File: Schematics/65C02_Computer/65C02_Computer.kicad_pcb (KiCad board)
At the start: 2 copper layers, 203.2 x 149.9 mm, 60 parts, among them J1 CLK Jumper, J2 Expansion port, J3 USB_B_Micro, J4 LCD Connector, J5 VIA2PA, J6 VIA2PB, J7 Mini-DIN-6, SW1 RESET, U1 74HC02, U10 FT230XS, U11 65C51N, U12 ATtiny4313-PU, U2 28C256, U3 65C02S, U4 74HC00, U5 74HC21, U6 62256, U7 NE555, U8 65C22S, U9 65C22S, X1 1MHz, X2 1.8432MHz

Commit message: Further updates to schematic
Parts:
- added R13: 4K7, Resistor_THT:R_Axial_DIN0207_L6.3mm_D2.5mm_P7.62mm_Horizontal, F.Cu at (137.5, 134.7)
- R1, R2, R4: value 3K3 -> 4K7
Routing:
- net +5V: track 295.5 -> 0.00 mm, vias 1 -> 0
- net a1: track 223.4 -> 0.00 mm
- net d4: track 223.4 -> 0.00 mm
- net a0: track 221.3 -> 0.00 mm, vias 2 -> 0
- net d5: track 220.5 -> 0.00 mm
- net d1: track 217.5 -> 0.00 mm
- net d6: track 216.0 -> 0.00 mm
- net d0: track 214.8 -> 0.00 mm
- net d2: track 214.1 -> 0.00 mm
- net a10: track 213.1 -> 0.00 mm
- net d7: track 212.5 -> 0.00 mm
- net d3: track 210.5 -> 0.00 mm
- net CLK: track 110.3 -> 0.00 mm, vias 2 -> 0
- net R~W: track 109.4 -> 0.00 mm, vias 3 -> 0
- net ~IOCS: track 106.3 -> 0.00 mm, vias 2 -> 0
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- removed copper zone on F.Cu, net GND

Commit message: Moved things around PCB
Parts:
- removed the REF** at (83.5, 205.5)
- moved C7 104.1 mm to (200.7, 78.7), turned to 270 degrees
- moved R13 100.6 mm to (193.0, 50.8)
- moved R6 86.2 mm to (143.5, 38.1), turned to 90 degrees
- moved C10 80.0 mm to (155.0, 50.8)
- moved R5 79.1 mm to (137.2, 38.1), turned to 90 degrees
- moved U5 79.0 mm to (40.6, 27.9)
- moved X1 77.9 mm to (33.0, 68.6)
- moved C6 76.4 mm to (73.7, 27.9), turned to 270 degrees
- moved J2 76.0 mm to (106.7, 53.3)
- moved R3 72.4 mm to (130.8, 38.1), turned to 90 degrees
- moved C8 70.3 mm to (137.2, 45.7), turned to 0 degrees
- moved C9 69.4 mm to (53.3, 28.0), turned to 270 degrees
- moved C4 62.6 mm to (128.3, 45.7), turned to 180 degrees
- moved U7 59.8 mm to (116.8, 38.1), turned to 90 degrees
- moved U1 59.2 mm to (81.3, 27.9)
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
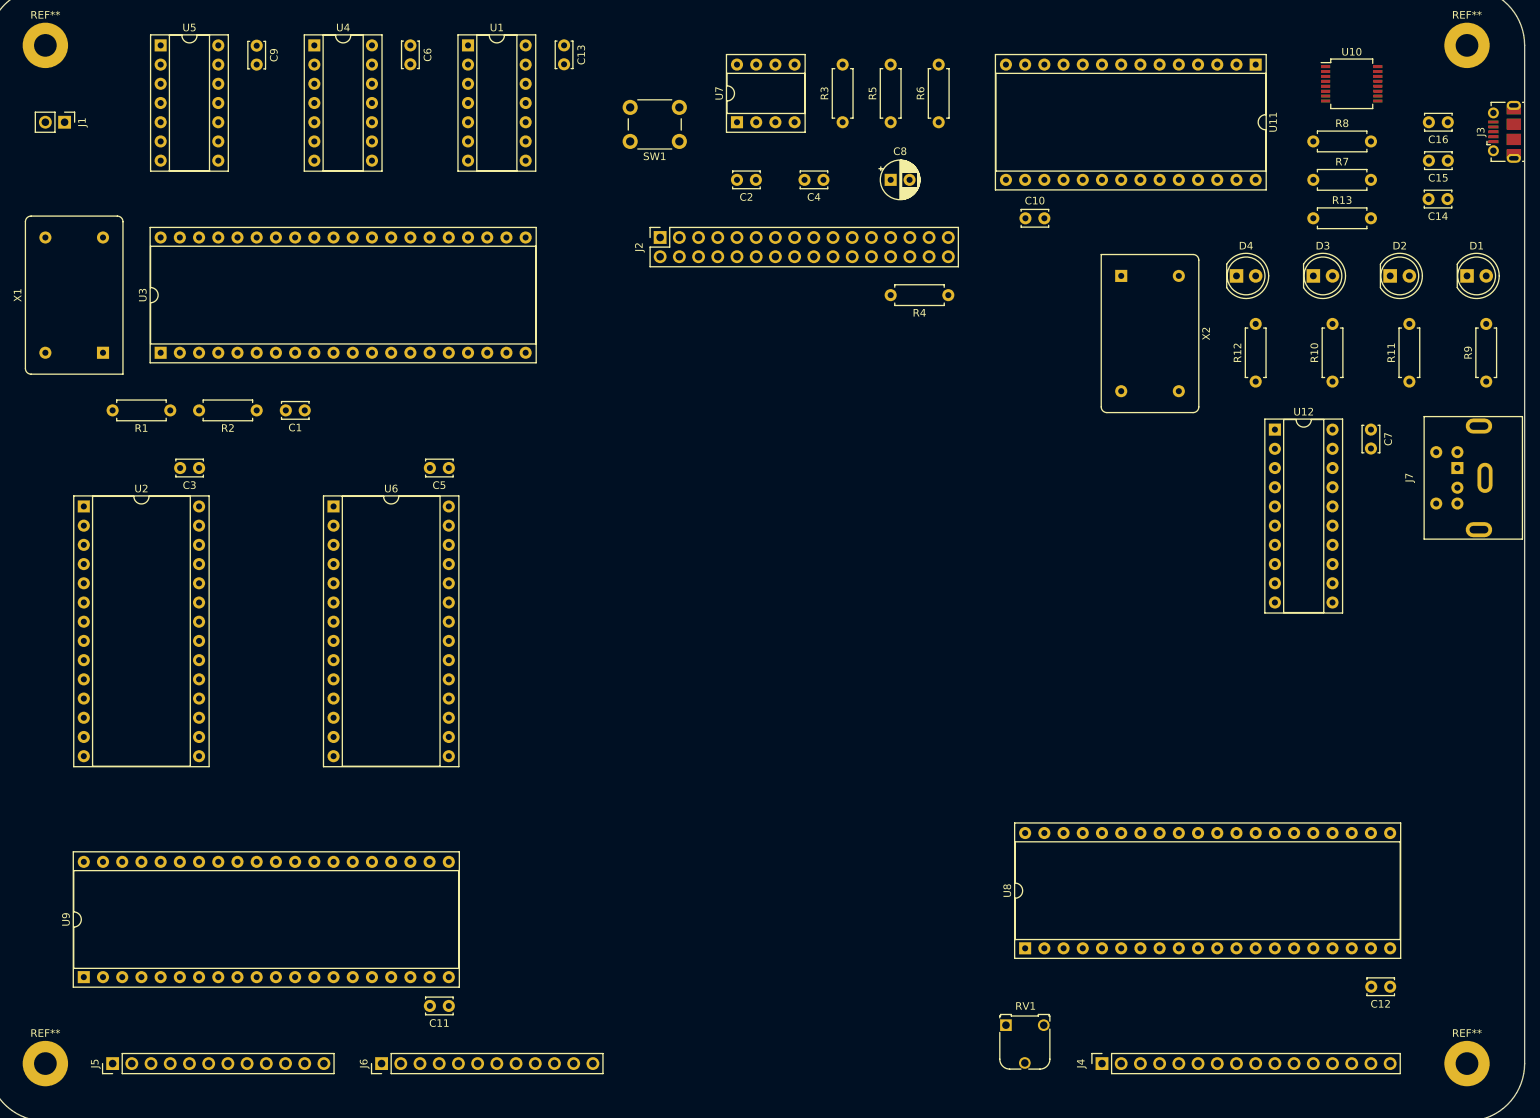
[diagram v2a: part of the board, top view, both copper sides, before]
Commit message: Some more tracks added
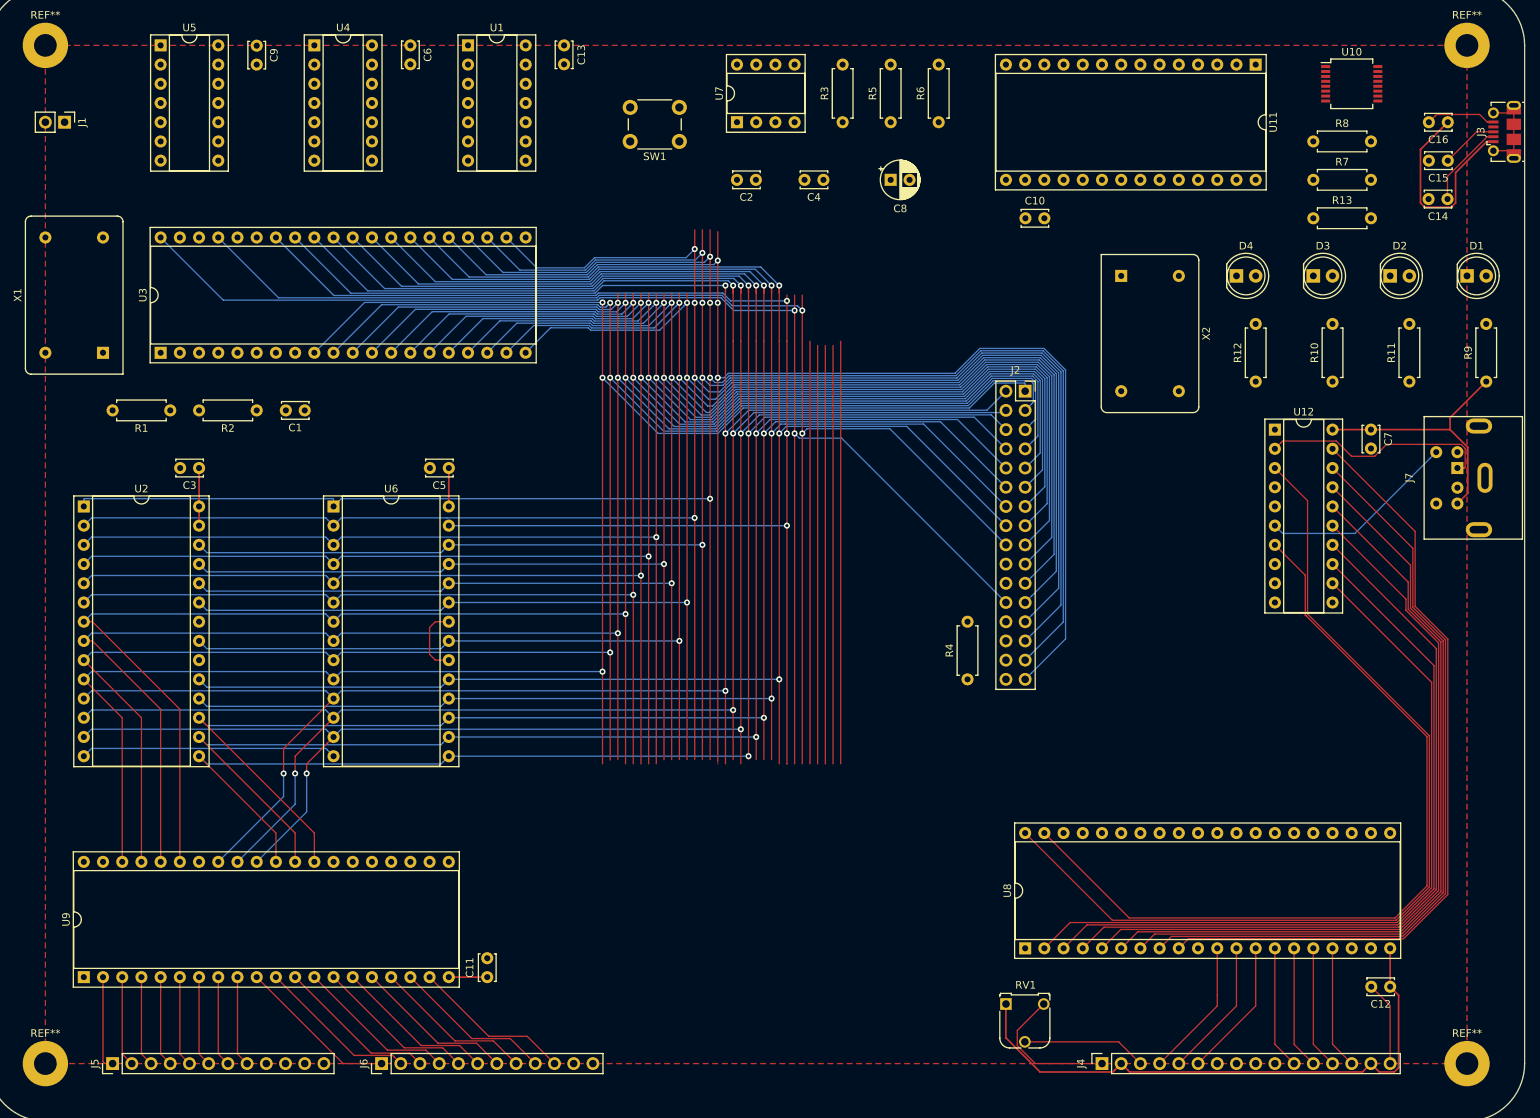
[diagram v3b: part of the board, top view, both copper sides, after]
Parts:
- moved J2 52.4 mm to (154.9, 73.7), turned to 0 degrees
- moved R4 50.9 mm to (147.3, 111.8), turned to 90 degrees
- moved C11 6.35 mm to (83.8, 151.1), turned to 90 degrees
- moved RV1 2.79 mm to (152.4, 154.7)
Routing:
- net a14: track 0.00 -> 280.2 mm, vias 0 -> 4
- net a3: track 0.00 -> 279.2 mm, vias 0 -> 3
- net d0: track 0.00 -> 278.1 mm, vias 0 -> 4
- net (no net): track 0.00 -> 277.7 mm
- net a2: track 0.00 -> 273.5 mm, vias 0 -> 3
- net d1: track 0.00 -> 271.6 mm, vias 0 -> 4
- net d2: track 0.00 -> 267.6 mm, vias 0 -> 4
- net a1: track 0.00 -> 266.5 mm, vias 0 -> 3
- net a12: track 0.00 -> 266.3 mm, vias 0 -> 4
- net a0: track 0.00 -> 260.7 mm, vias 0 -> 3
- net a13: track 0.00 -> 256.8 mm, vias 0 -> 4
- net d5: track 0.00 -> 253.8 mm, vias 0 -> 3
- net d4: track 0.00 -> 251.0 mm, vias 0 -> 3
- net d3: track 0.00 -> 248.1 mm, vias 0 -> 3
- net a7: track 0.00 -> 247.6 mm, vias 0 -> 3
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- added copper zone on F.Cu, net GND

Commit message: Almost done...
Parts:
- moved C4 9.25 mm to (119.4, 43.2)
- moved R13 7.62 mm to (200.7, 50.5), turned to 180 degrees
- moved C2 5.72 mm to (124.5, 43.2)
- moved C10 2.58 mm to (152.4, 50.8)
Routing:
- net +5V: track 157.5 -> 762.8 mm, vias 0 -> 2
- net ~IOCS: track 0.00 -> 360.6 mm, vias 0 -> 5
- net ~RES: track 187.3 -> 544.9 mm, vias 2 -> 9
- net (no net): track 277.7 -> 0.00 mm
- net CLK: track 177.0 -> 431.4 mm, vias 2 -> 7
- net ~V1IRQ: track 0.00 -> 249.7 mm, vias 0 -> 2
- net R~W: track 178.0 -> 417.8 mm, vias 3 -> 7
- net ~ROM_OE: track 0.00 -> 218.6 mm, vias 0 -> 3
- net ~ROM_CS: track 0.00 -> 214.9 mm, vias 0 -> 1
- net d7: track 227.6 -> 430.9 mm, vias 3 -> 6
- net d6: track 227.7 -> 430.4 mm, vias 3 -> 6
- net ~RAM_CS: track 9.27 -> 188.5 mm, vias 0 -> 3
- net ~IRQX: track 0.00 -> 171.2 mm, vias 0 -> 6
- net ~AIRQ: track 0.00 -> 164.9 mm, vias 0 -> 2
- net d5: track 253.8 -> 391.2 mm, vias 3 -> 5
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- added copper zone on B.Cu, net GND

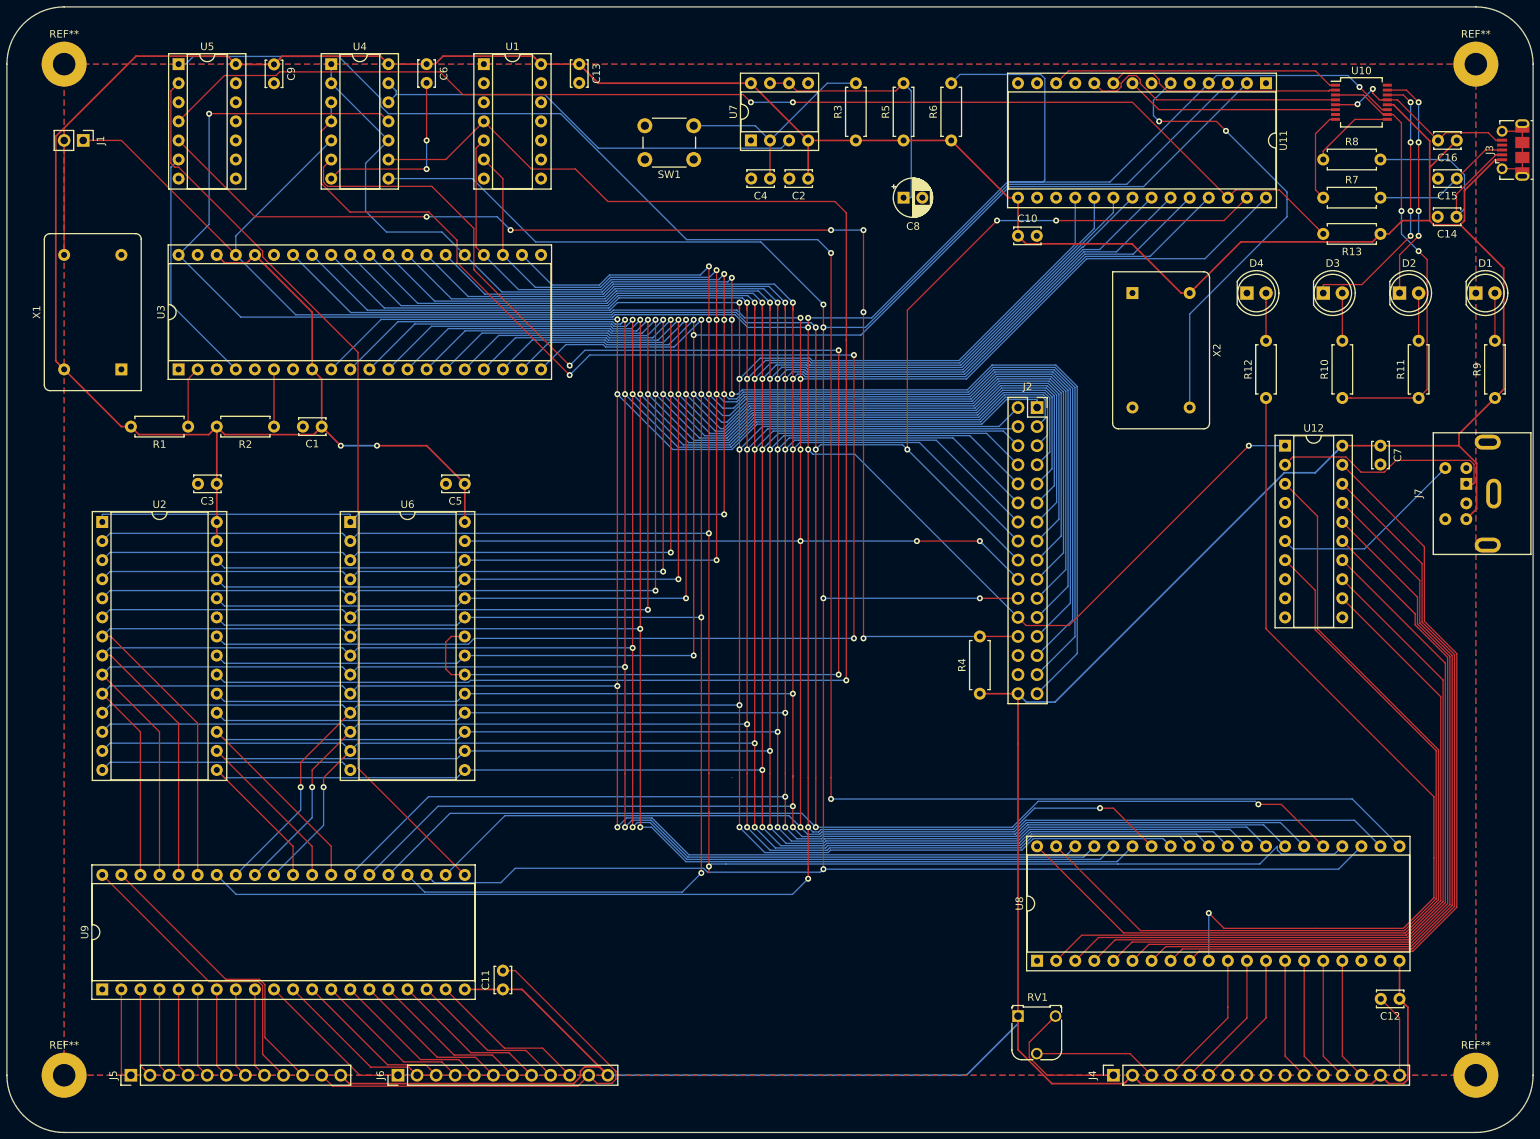
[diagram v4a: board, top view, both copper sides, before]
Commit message: All tracks placed on PCB, DRC fine
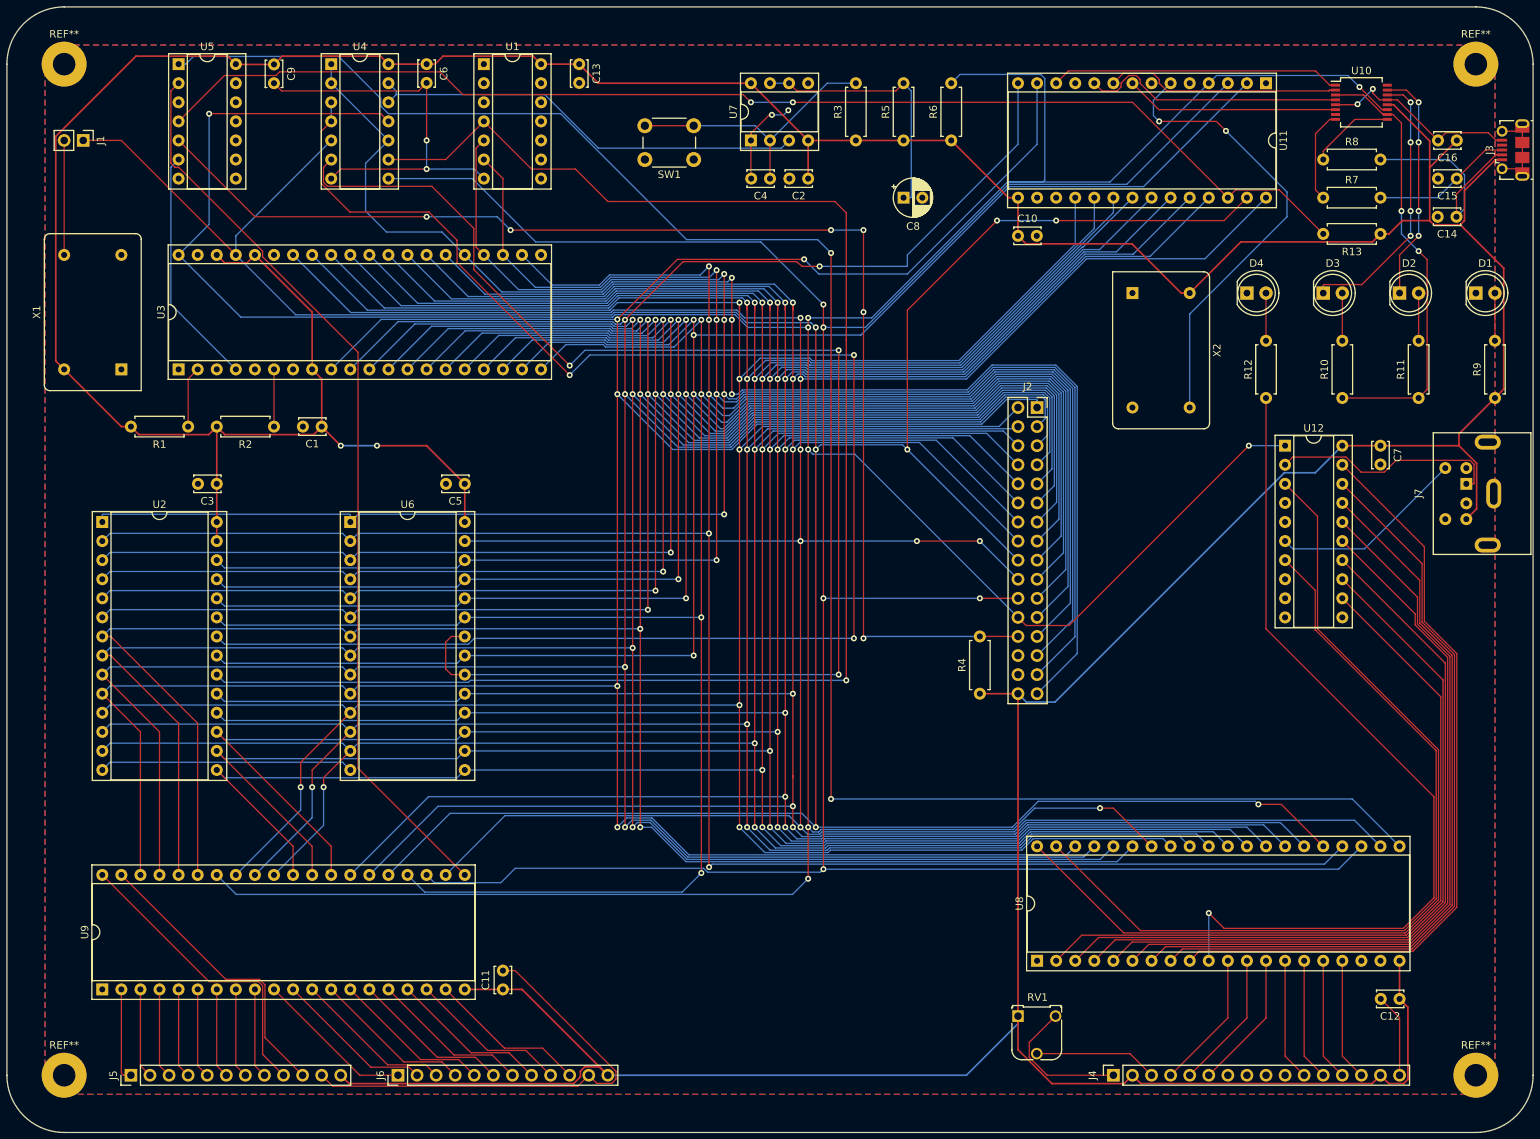
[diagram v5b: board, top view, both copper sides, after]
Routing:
- net a0: track 331.3 -> 406.6 mm, vias 4 -> 5
- net a1: track 339.2 -> 410.9 mm, vias 4 -> 5
- net GND: track 178.7 -> 220.3 mm, vias 4 -> 6
- net Net-(C4-Pad1): track 30.6 -> 37.1 mm
- net a12: track 363.5 -> 361.7 mm

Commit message: Basic annotations added
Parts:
- moved R4 5.08 mm to (142.2, 111.8)
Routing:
- net +5V: track 762.8 -> 767.8 mm
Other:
- board text added: "+5V"
- board text added: "1.8432 MHz Serial Clock"
- board text added: "1MHz System Clock"
- board text added: "A"
- board text added: "A00"
- board text added: "A01"
- board text added: "A02"
- board text added: "A03"
- board text added: "A04"
- board text added: "A05"
- board text added: "A06"
- board text added: "A07"
- board text added: "A08"
- board text added: "A09"
- board text added: "A10"
- board text added: "A11"
- board text added: "A12"
- board text added: "A13"
- board text added: "A14"
- board text added: "A15"
- board text added: "Address Bus"
- board text added: "Address Decoder"
- board text added: "Asynchronous Communication Interface Adapter"
- board text added: "Blink"
- board text added: "CA1"
- board text added: "CA2"
- board text added: "CB1"
- board text added: "CB2"
- board text added: "CLK"
- board text added: "CLK IN"
- board text added: "Central Processing Unit"
- board text added: "Control Signals"
- board text added: "D0"
- board text added: "D1"
- board text added: "D2"
- board text added: "D3"
- board text added: "D4"
- board text added: "D5"
- board text added: "D6"
- board text added: "D7"
- board text added: "DB0"
- board text added: "DB1"
- board text added: "DB2"
- board text added: "DB3"
- board text added: "DB4"
- board text added: "DB5"
- board text added: "DB6"
- board text added: "DB7"
- board text added: "Data Bus"
- board text added: "E"
- board text added: "External Clock Connector"
- board text added: "GND"
- board text added: "Interrupt Handler"
- board text added: "K"
- board text added: "Keyboard Connector PS/2"
- board text added: "Keyboard Controller"
- board text added: "LCD Connector"
- board text added: "LCD Contrast"
- board text added: "NC"
- board text added: "PA0"
- board text added: "PA1"
- board text added: "PA2"
- board text added: "PA3"
- board text added: "PA4"
- board text added: "PA5"
- board text added: "PA6"
- board text added: "PA7"
- board text added: "PB0"
- board text added: "PB1"
- board text added: "PB2"
- board text added: "PB3"
- board text added: "PB4"
- board text added: "PB5"
- board text added: "PB6"
- board text added: "PB7"
- board text added: "Power"
- board text added: "RS"
- board text added: "Random Access Memory"
- board text added: "Read Only Memory"
- board text added: "Receive"
- board text added: "R~W"
- board text added: "System Reset"
- board text added: "Transmit"
- board text added: "USB"
- board text added: "USB Interface"
- board text added: "VDD"
- board text added: "VO"
- board text added: "VSS"
- board text added: "Versatile Interface Adapter #1"
- board text added: "Versatile Interface Adapter #2"
- board text added: "~IOCS"
- board text added: "~IRQ"
- board text added: "~RES"
